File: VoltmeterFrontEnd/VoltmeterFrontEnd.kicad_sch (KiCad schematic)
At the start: 23 parts, among them J1 Voltmeter, J15 Barrel_Jack, Q3 MMBT3904, Q8 AO3400A MOSFET, SW3 SW_Push, U10 LM4040DBZ-2.5, U7 MAX1683

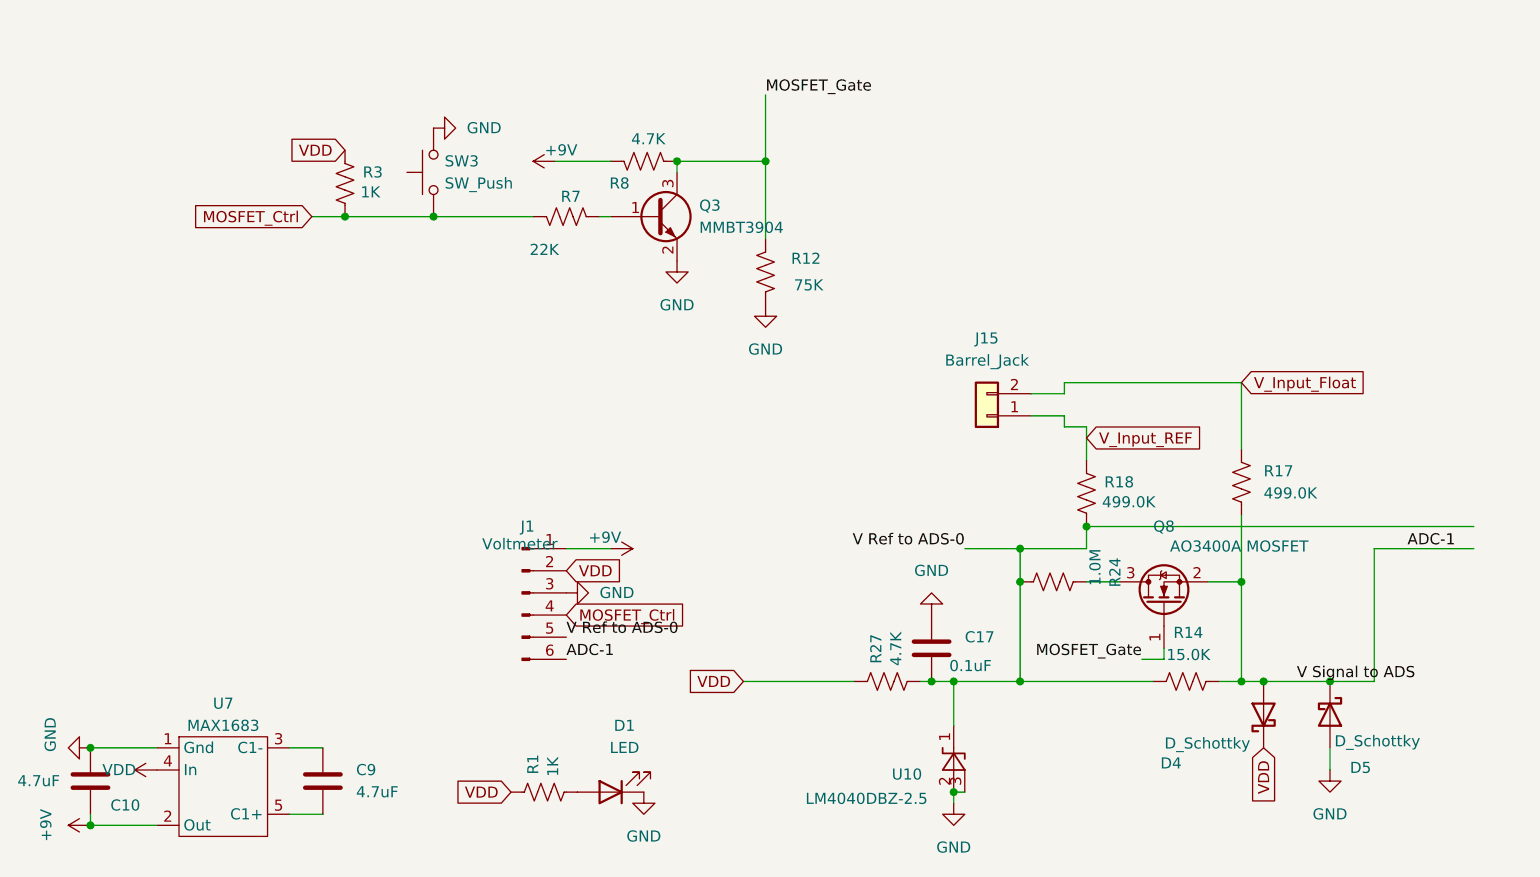
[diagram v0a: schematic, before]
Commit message: Finishing PCBs to be made.
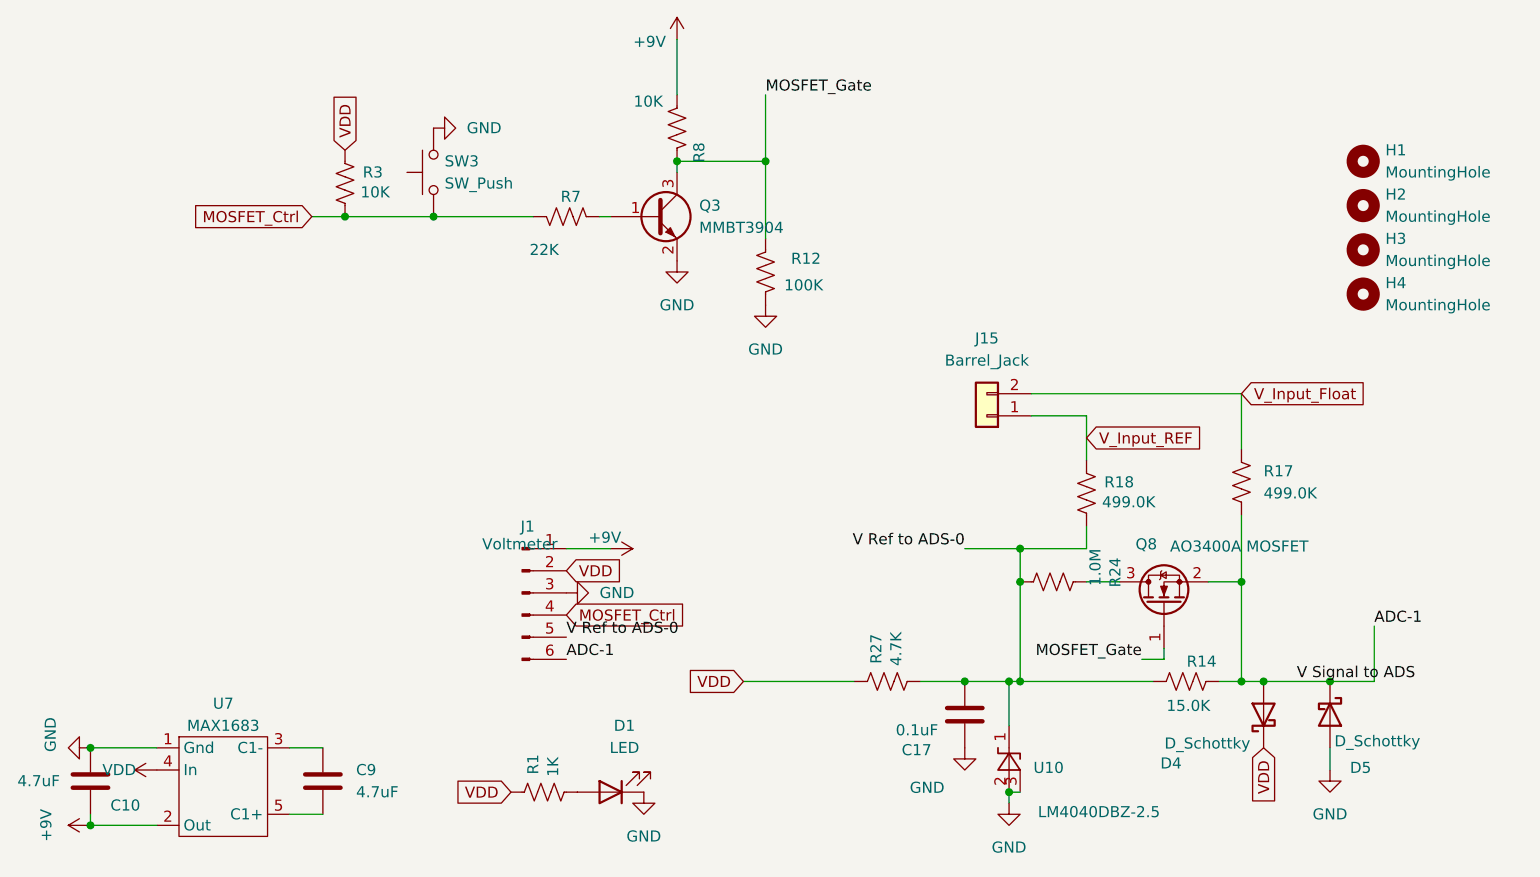
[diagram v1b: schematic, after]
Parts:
- added H1, H2, H3, H4: MountingHole, MountingHole:MountingHole_3.2mm_M3_DIN965_Pad_TopBottom, symbol Mechanical:MountingHole
- R12: value 75K -> 100K
- R3: value 1K -> 10K
- R8: value 4.7K -> 10K
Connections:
- net +9V: now also R8.2; no longer R8.1
- net MOSFET_Gate: now also R8.1; no longer R8.2
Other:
- moved on the sheet: C17, R8, U10

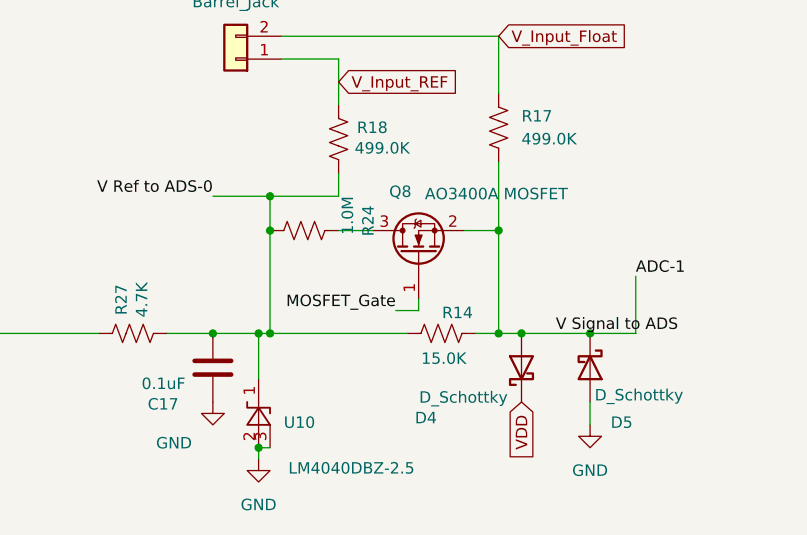
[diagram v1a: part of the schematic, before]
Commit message: Further process meter w/ open lead detect work
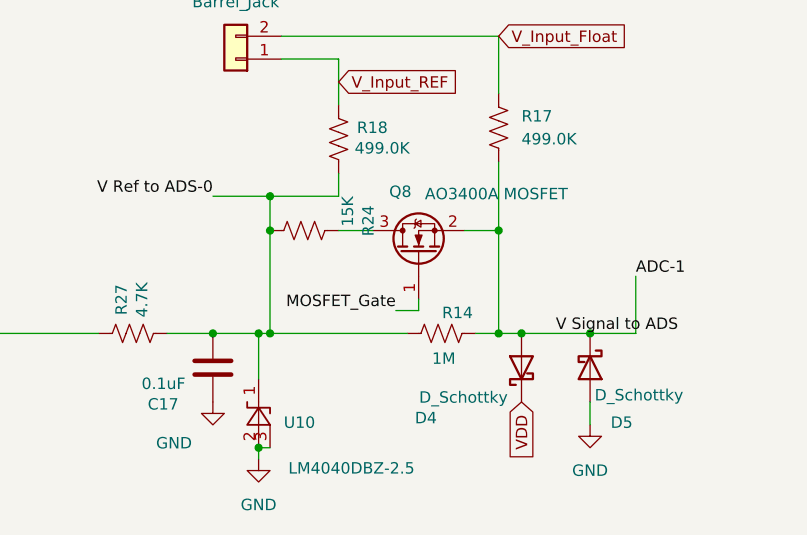
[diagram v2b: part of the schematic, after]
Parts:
- R14: value 15.0K -> 1M
- R24: value 1.0M -> 15K
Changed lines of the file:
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@@
 			)
 		)
-		(property "Value" "15.0K"
+		(property "Value" "1M"
 			(at 157.734 100.584 90)
 			(effects
@@
 			)
 		)
-		(property "Value" "1.0M"
+		(property "Value" "15K"
 			(at 147.066 82.55 0)
 			(effects
